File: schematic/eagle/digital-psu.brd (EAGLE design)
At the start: 107.6 x 85.1 mm, 79 parts, among them IC1 TL072P, IC2 TLC272P, Q1 MPSA56-TO92, T3 2N3055, T4 2N3055, T5 2N3055, X1 Vout, X2 PASS_TRANSISTORS, X3 AC_IN

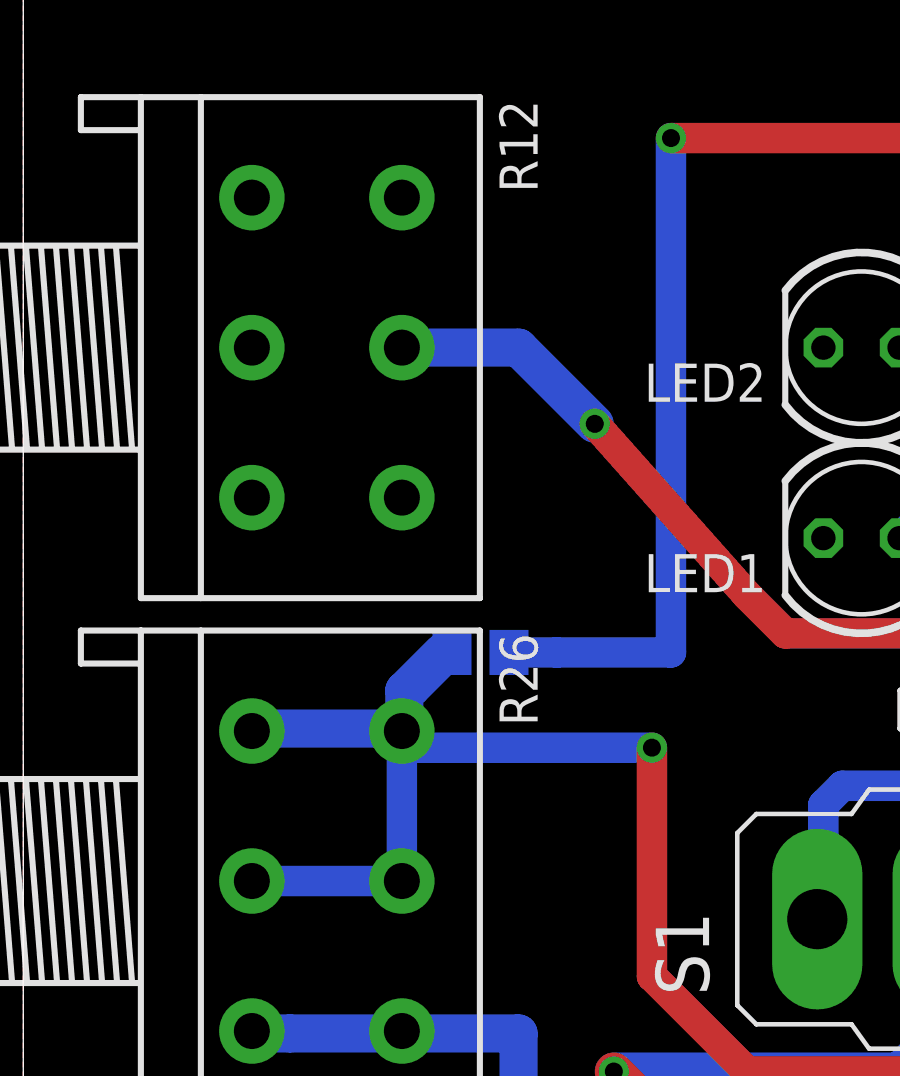
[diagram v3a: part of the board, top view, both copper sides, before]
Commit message: developed common-mode extending current sensor daughter board eagle + gerbers
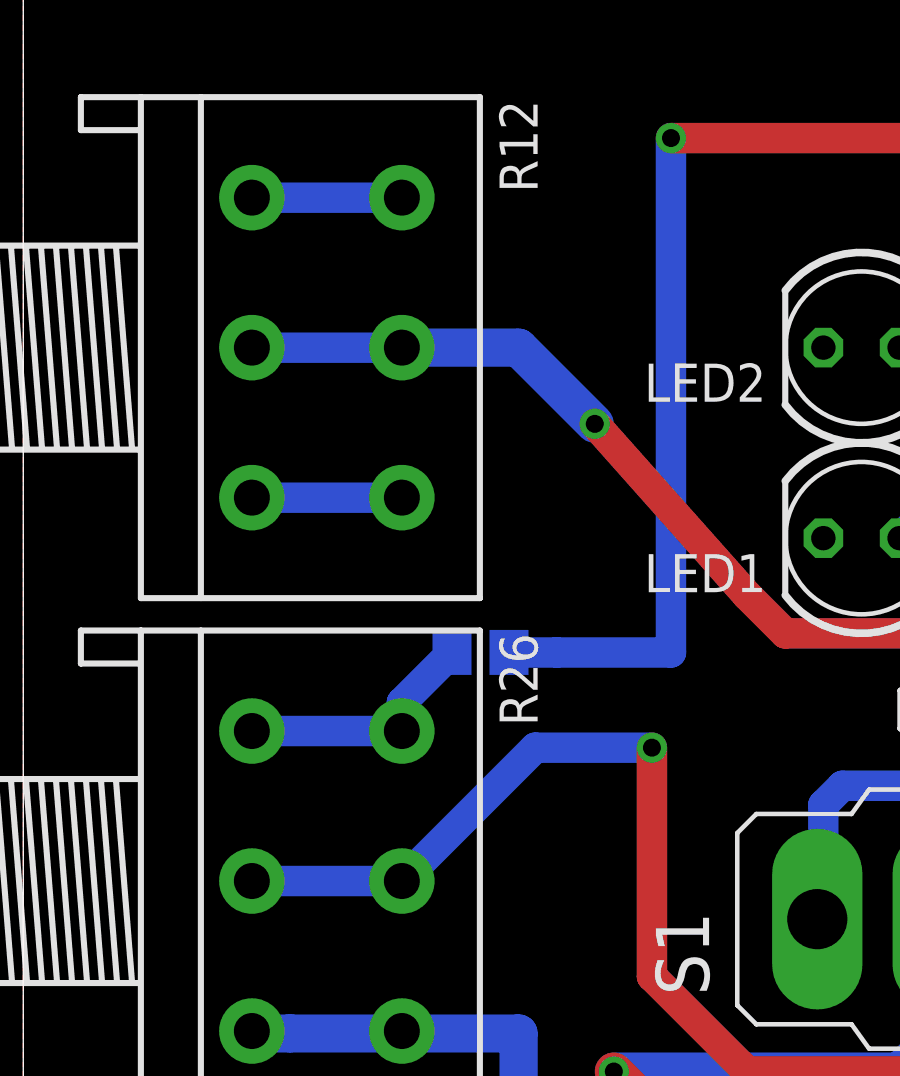
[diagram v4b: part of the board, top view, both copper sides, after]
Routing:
- net N$5: track 8.15 -> 0.00 mm
- net N$32: track 0.00 -> 5.11 mm
- net N$20: track 9.02 -> 14.0 mm
- net ADJ_CURR: track 51.8 -> 56.8 mm
- net ADJ_VOLT: track 89.8 -> 86.7 mm
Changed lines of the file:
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@@
 <wire x1="27.94" y1="55.245" x2="30.48" y2="55.245" width="0" layer="19" extent="1-1"/>
 <wire x1="63.5" y1="72.07" x2="51.12" y2="74.93" width="0" layer="19" extent="16-16"/>
-<wire x1="25.4" y1="30.48" x2="27.94" y2="55.245" width="0" layer="19" extent="1-1"/>
 <wire x1="57.15" y1="17.46" x2="45.72" y2="3.81" width="0" layer="19" extent="16-16"/>
 <wire x1="54.93" y1="46.99" x2="30.48" y2="55.245" width="0" layer="19" extent="16-16"/>
@@
 <contactref element="R12" pad="1-3"/>
 <contactref element="R12" pad="2-3"/>
+<wire x1="5.08" y1="62.31" x2="10.08" y2="62.31" width="1.016" layer="16"/>
 <wire x1="10.08" y1="62.31" x2="53.34" y2="66.04" width="0" layer="19" extent="1-1"/>
-<wire x1="5.08" y1="62.31" x2="10.08" y2="62.31" width="0" layer="19" extent="1-1"/>
 </signal>
 <signal name="N$23">
@@
 <wire x1="16.51" y1="64.77" x2="21.59" y2="59.055" width="1.016" layer="1"/>
 <contactref element="R12" pad="1-2"/>
-<wire x1="5.08" y1="67.31" x2="10.08" y2="67.31" width="0" layer="19" extent="1-1"/>
+<wire x1="10.08" y1="67.31" x2="5.08" y2="67.31" width="1.016" layer="16"/>
 </signal>
 <signal name="N$24" airwireshidden="yes">
@@
 <wire x1="18.415" y1="46.355" x2="18.415" y2="53.975" width="1.016" layer="1"/>
 <via x="18.415" y="53.975" extent="1-16" drill="0.6" shape="square"/>
-<wire x1="18.415" y1="53.975" x2="10.16" y2="53.975" width="1.016" layer="16"/>
-<wire x1="10.16" y1="53.975" x2="10.16" y2="54.45" width="1.016" layer="16"/>
 <contactref element="R26" pad="2-2"/>
 <contactref element="R26" pad="1-2"/>
 <wire x1="5.08" y1="49.53" x2="10.08" y2="49.53" width="1.016" layer="16"/>
-<wire x1="10.08" y1="49.53" x2="10.08" y2="53.895" width="1.016" layer="16"/>
-<wire x1="10.08" y1="53.895" x2="10.16" y2="53.975" width="1.016" layer="16"/>
+<wire x1="18.415" y1="53.975" x2="14.525" y2="53.975" width="1.016" layer="16"/>
+<wire x1="14.525" y1="53.975" x2="10.08" y2="49.53" width="1.016" layer="16"/>
 </signal>
 <signal name="N$4">
@@
 </signal>
 <signal name="N$5">
-<wire x1="5.08" y1="54.61" x2="10.16" y2="54.61" width="1.27" layer="16"/>
-<wire x1="10.16" y1="54.61" x2="10.16" y2="55.88" width="1.27" layer="16"/>
-<wire x1="10.16" y1="55.88" x2="11.43" y2="57.15" width="1.27" layer="16"/>
 </signal>
 <signal name="N$41">
@@
 <contactref element="IC2" pad="6"/>
 <contactref element="C14" pad="2"/>
-<wire x1="10.08" y1="54.53" x2="5.08" y2="54.53" width="1.016" layer="16"/>
-<wire x1="10.08" y1="54.53" x2="10.08" y2="55.8" width="1.016" layer="16"/>
-<wire x1="10.08" y1="55.8" x2="10.16" y2="55.88" width="1.016" layer="16"/>
-<wire x1="10.16" y1="55.88" x2="10.48" y2="55.88" width="1.016" layer="16"/>
-<wire x1="10.48" y1="55.88" x2="11.75" y2="57.15" width="1.016" layer="16"/>
 <wire x1="68.58" y1="62.23" x2="68.58" y2="62.865" width="1.016" layer="16"/>
 <wire x1="68.58" y1="62.865" x2="71.755" y2="66.04" width="1.016" layer="16"/>
@@
 <wire x1="68.58" y1="62.865" x2="68.26" y2="66.04" width="0" layer="19" extent="16-16"/>
 <wire x1="11.75" y1="57.15" x2="68.58" y2="62.23" width="0" layer="19" extent="16-16"/>
+<wire x1="5.08" y1="54.53" x2="10.08" y2="54.53" width="1.016" layer="16"/>
+<wire x1="10.08" y1="54.53" x2="10.08" y2="55.48" width="1.016" layer="16"/>
+<wire x1="10.08" y1="55.48" x2="11.75" y2="57.15" width="1.016" layer="16"/>
 </signal>
 <signal name="N$32">
@@
 <contactref element="R13" pad="1"/>
 <contactref element="R12" pad="2-1"/>
-<wire x1="10.08" y1="72.31" x2="53.02" y2="74.93" width="0" layer="19" extent="16-16"/>
-<wire x1="5.08" y1="72.31" x2="10.08" y2="72.31" width="0" layer="19" extent="1-1"/>
+<wire x1="5.08" y1="72.31" x2="10.08" y2="72.31" width="1.016" layer="16"/>
+<wire x1="10.08" y1="72.31" x2="10.16" y2="72.39" width="1.016" layer="16"/>
+<wire x1="10.16" y1="72.39" x2="53.02" y2="74.93" width="0" layer="19" extent="16-16"/>
 </signal>
 </signals>
